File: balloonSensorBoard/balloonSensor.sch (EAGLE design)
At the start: 36 parts, among them IC1 MCP601OT, IC10 MCP601OT, IC6 MCP601OT, IC7 MCP601OT, U1 ARDUINO-MEGAPRO

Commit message: updated .sch, .brd
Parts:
- removed +9V1: 500 ohm, rcl:R-US_R1206
- removed C6, C7: 10uF, resistor:CPOL-EUCT3216
- removed LD1085: (no value), v-reg:LM138-TL
- removed LED3: (no value), SparkFun:LED3MM
- removed U$3: XBEE-1B3, SparkFun:XBEE-1B3
- added C2: 100nF, resistor:CPOL-EUCT3216
- added C3: 10uF, resistor:CPOL-EUCT3216
- added JP1: (no value), SparkFun:M04LONGPADS
- added LD1117: V_REG_317SMD, SparkFun:V_REG_317SMD
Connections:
- removed net N$19: +9V1.2, LED3.C
- net +3V3: now also JP1.1, U1.3.3V; no longer U$3.VDD
- net +9V: now also C2.+, LD1117.IN, U1.VIN; no longer C6.+, LD1085.IN
- net GND: now also C2.-, C3.-, JP1.4, LD1117.ADJ, U1.GND@4; no longer +9V1.1, C6.-, C7.-, LD1085.ADJ, U$3.GND
- net N$13: now also JP1.3; no longer U$3.DIN
- net N$5: now also JP1.2; no longer U$3.DOUT
- net V+: now also C3.+, LD1117.OUT; no longer C7.+, LD1085.OUT, LED3.A
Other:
- note added: "1.8v"
- note added: "XBee"
- note added: "temp/humidity"
- moved on the sheet: C1, JP4, R1, R4

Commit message: added sensors and miscellaneous parts and routed board
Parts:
- removed IC1, IC10, IC6, IC7: MCP601OT, linear:MCP601OT
- removed JP5: (no value), SparkFun:M04LONGPADS
- removed JP6: (no value), jumper:JP1Q
- removed TP1, TP2: TPPAD1-13Y, testpad:TPPAD1-13Y
- added BAROMETER: (no value), SparkFun:M07LONGPADS
- added COMPASS: COMPASS, balloonshield:COMPASS
- added R6: 1k, rcl:R-US_R1206
- renumbered JP1 to XBEE, JP2 to WINDSPEED, JP4 to DUST, U$1 to VOC, U$13 to CO, U$14 to TEMP/HUMIDITY, U$9 to O3
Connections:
- removed net N$12: JP5.3, U1.20(SDA)
- removed net N$20: JP5.4, U1.21(SCL)
- removed net N$48: IC10.-IN, IC10.OUT, U1.A1(TX0)
- removed net N$52: IC6.-IN, IC6.OUT, U1.A0(RX0)
- removed net N$9: IC7.-IN, IC7.OUT, U1.A2
- new net 5V: R1.2, TEMP/HUMIDITY.VDD, U1.5V@0, U1.5V@1, U1.5V@2
- new net SCL: BAROMETER.3, COMPASS.SCL, U1.21(SCL)
- new net SDA: BAROMETER.4, COMPASS.SDA, U1.20(SDA)
- net +3V3: no longer JP5.2
- net +9V: now also BAROMETER.1, COMPASS.VIN
- net GND: now also BAROMETER.7, COMPASS.GND; no longer IC1.V-, IC10.V-, IC6.V-, IC7.V-, JP5.1, TP2.TP
- net N$2: now also U1.A3; no longer IC1.+IN
- net N$4: now also R6.1, U1.AREF; no longer IC1.-IN, IC1.OUT, U1.A3
- net N$47: now also U1.A1(TX0); no longer IC10.+IN
- net N$50: now also U1.A0(RX0); no longer IC6.+IN
- net N$55: now also U1.A2; no longer IC7.+IN
- net V+: now also R6.2; no longer IC1.V+, IC10.V+, IC6.V+, IC7.V+, JP6.1, JP6.2, R1.2, TEMP/HUMIDITY.VDD, TP1.TP
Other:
- note added: "VOC"
- note added: "barometer (altitude)"
- note added: "compass (wind direction)"
- note added: "wind speed"
- note removed: "V+/5V TEST PADS"
- note removed: "compass"
- note removed: "wind"

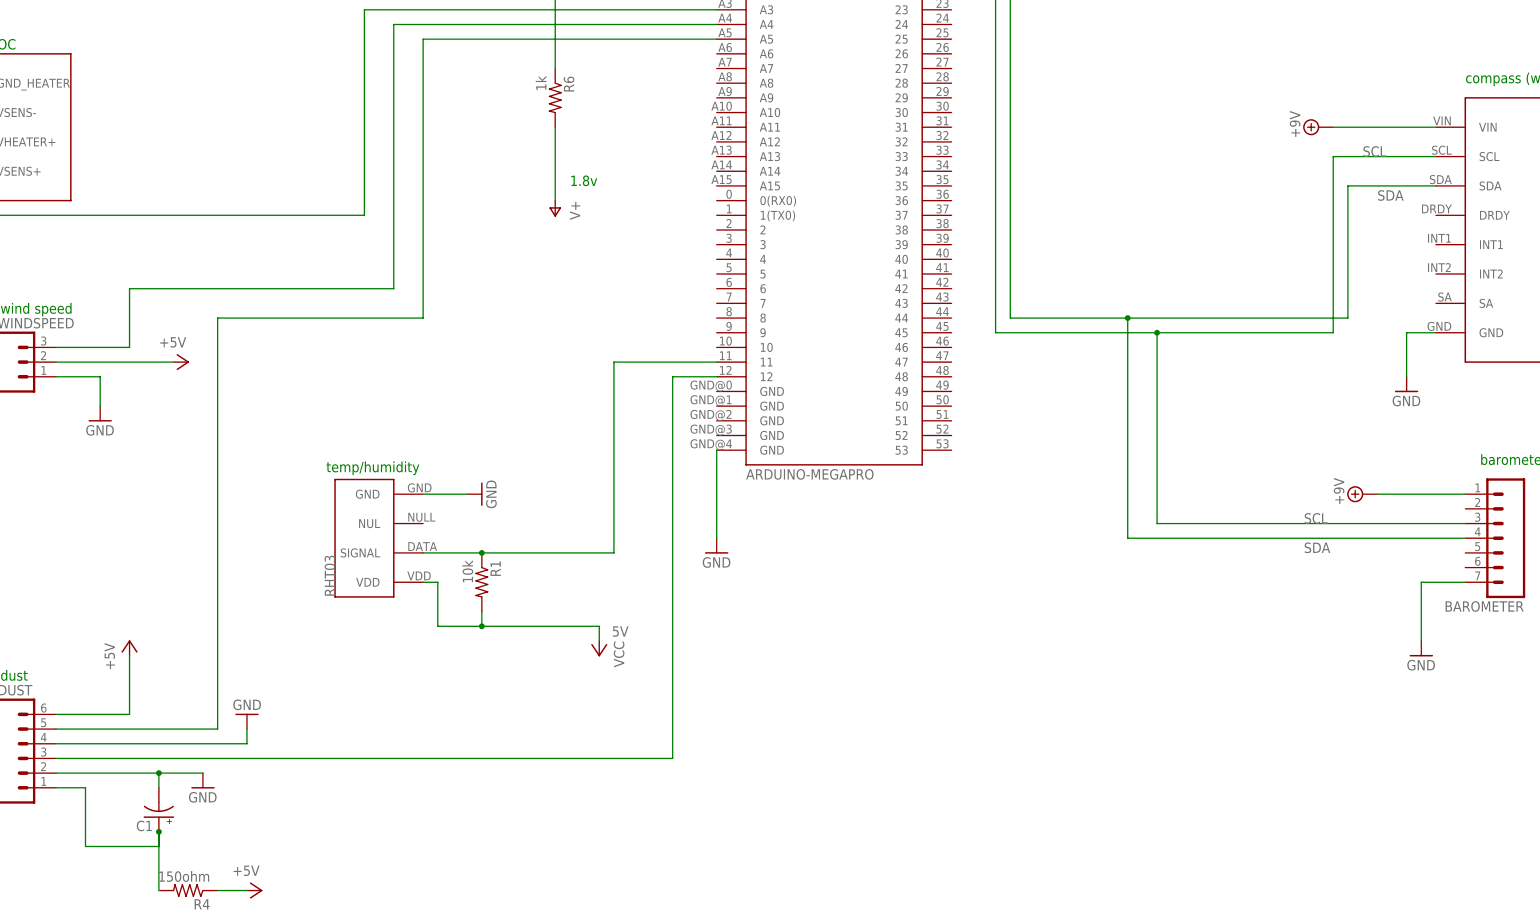
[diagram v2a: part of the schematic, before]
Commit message: added cap size, mod a couple vins
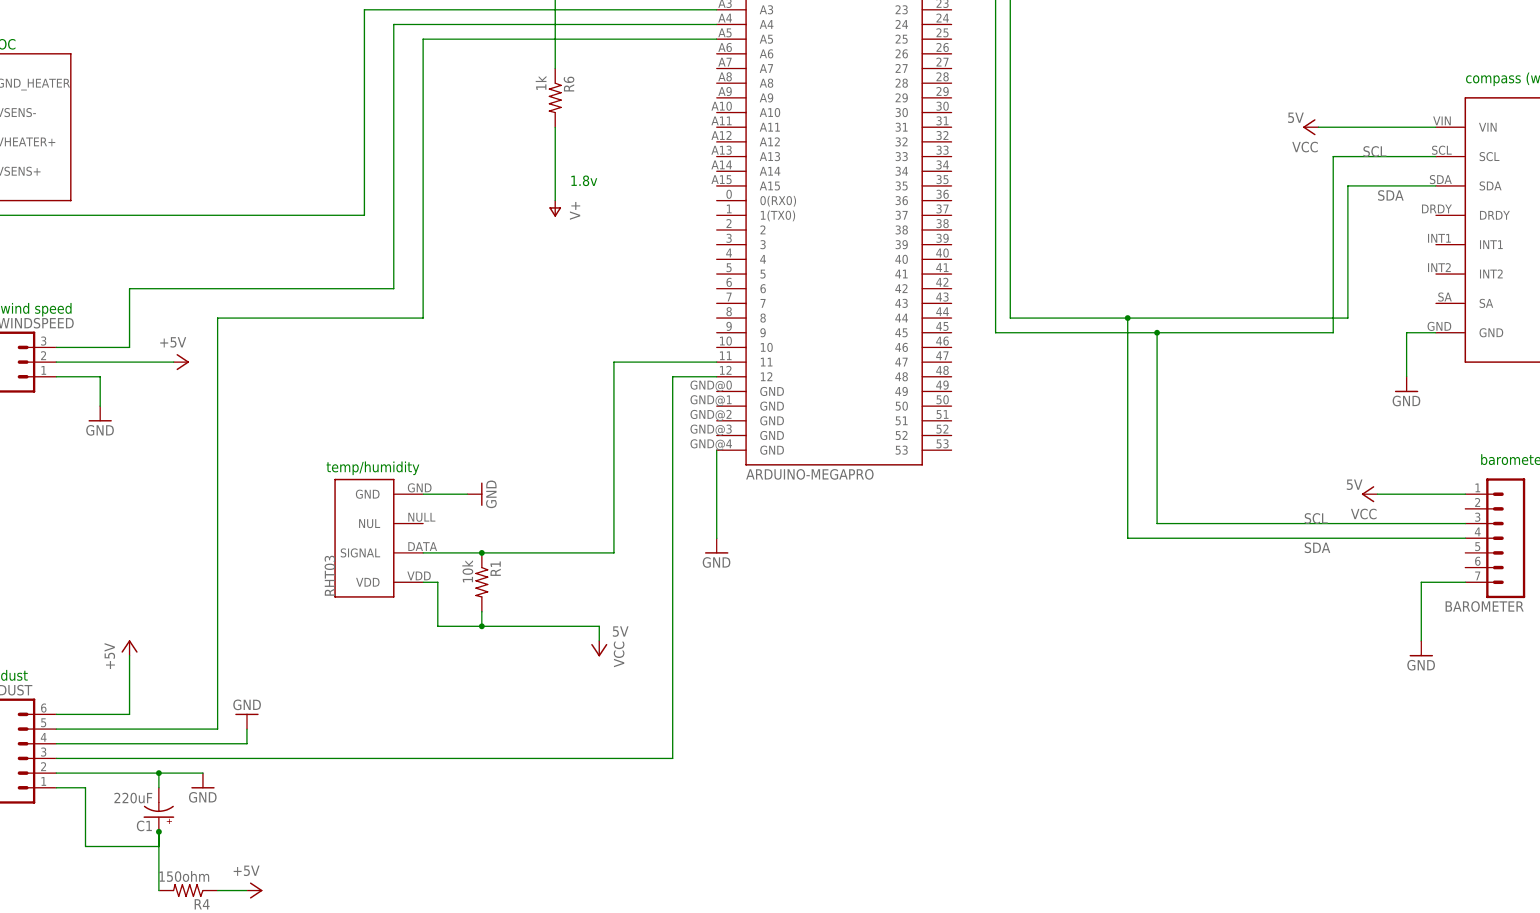
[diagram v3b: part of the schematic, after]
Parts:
- C1: value (none) -> 220uF
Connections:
- new net VCC: BAROMETER.1, COMPASS.VIN
- net +9V: no longer BAROMETER.1, COMPASS.VIN
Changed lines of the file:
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@@
 <part name="GND10" library="supply1" deviceset="GND" device=""/>
 <part name="R4" library="rcl" deviceset="R-US_" device="R1206" value="150ohm"/>
-<part name="C1" library="SparkFun" deviceset="CAP_POL" device="7343"/>
+<part name="C1" library="SparkFun" deviceset="CAP_POL" device="7343" value="220uF"/>
 <part name="GND11" library="supply1" deviceset="GND" device=""/>
 <part name="+3V2" library="supply1" deviceset="+3V3" device=""/>
@@
 <part name="COMPASS" library="balloonshield" deviceset="COMPASS" device=""/>
 <part name="5V" library="supply1" deviceset="VCC" device=""/>
-<part name="SUPPLY4" library="supply2" deviceset="+9V" device=""/>
-<part name="SUPPLY5" library="supply2" deviceset="+9V" device=""/>
 <part name="GND1" library="supply1" deviceset="GND" device=""/>
 <part name="5V1" library="supply1" deviceset="VCC" device=""/>
 <part name="P+1" library="supply1" deviceset="V+" device=""/>
 <part name="R6" library="rcl" deviceset="R-US_" device="R1206" value="1k"/>
+<part name="5V2" library="supply1" deviceset="VCC" device=""/>
+<part name="5V3" library="supply1" deviceset="VCC" device=""/>
 </parts>
 <sheets>
@@
 <instance part="COMPASS" gate="G$1" x="294.64" y="106.68"/>
 <instance part="5V" gate="VCC" x="137.16" y="160.02"/>
-<instance part="SUPPLY4" gate="G$1" x="271.78" y="53.34" rot="R90"/>
-<instance part="SUPPLY5" gate="G$1" x="264.16" y="116.84" rot="R90"/>
 <instance part="GND1" gate="1" x="281.94" y="25.4"/>
 <instance part="5V1" gate="VCC" x="139.7" y="25.4" rot="R180"/>
 <instance part="P+1" gate="1" x="132.08" y="101.6" rot="R180"/>
 <instance part="R6" gate="G$1" x="132.08" y="121.92" rot="R270"/>
+<instance part="5V2" gate="VCC" x="271.78" y="53.34" rot="R90"/>
+<instance part="5V3" gate="VCC" x="261.62" y="116.84" rot="R90"/>
 </instances>
 <busses>
@@
 <wire x1="302.26" y1="256.54" x2="294.64" y2="256.54" width="0.1524" layer="91"/>
 <junction x="294.64" y="256.54"/>
-</segment>
-<segment>
-<pinref part="SUPPLY4" gate="G$1" pin="+9V"/>
-<wire x1="274.32" y1="53.34" x2="289.56" y2="53.34" width="0.1524" layer="91"/>
-<pinref part="BAROMETER" gate="G$1" pin="1"/>
-</segment>
-<segment>
-<pinref part="SUPPLY5" gate="G$1" pin="+9V"/>
-<wire x1="266.7" y1="116.84" x2="284.48" y2="116.84" width="0.1524" layer="91"/>
-<pinref part="COMPASS" gate="G$1" pin="VIN"/>
 </segment>
 </net>
@@
 <wire x1="111.76" y1="30.48" x2="119.38" y2="30.48" width="0.1524" layer="91"/>
 <junction x="119.38" y="30.48"/>
+<label x="271.78" y="55.88" size="1.778" layer="95" rot="R180"/>
+<label x="261.62" y="119.38" size="1.778" layer="95" rot="R180"/>
 </segment>
 </net>
@@
 </segment>
 </net>
+<net name="VCC" class="0">
+<segment>
+<wire x1="274.32" y1="53.34" x2="289.56" y2="53.34" width="0.1524" layer="91"/>
+<pinref part="BAROMETER" gate="G$1" pin="1"/>
+<pinref part="5V2" gate="VCC" pin="VCC"/>
+</segment>
+<segment>
+<wire x1="264.16" y1="116.84" x2="284.48" y2="116.84" width="0.1524" layer="91"/>
+<pinref part="COMPASS" gate="G$1" pin="VIN"/>
+<pinref part="5V3" gate="VCC" pin="VCC"/>
+</segment>
+</net>

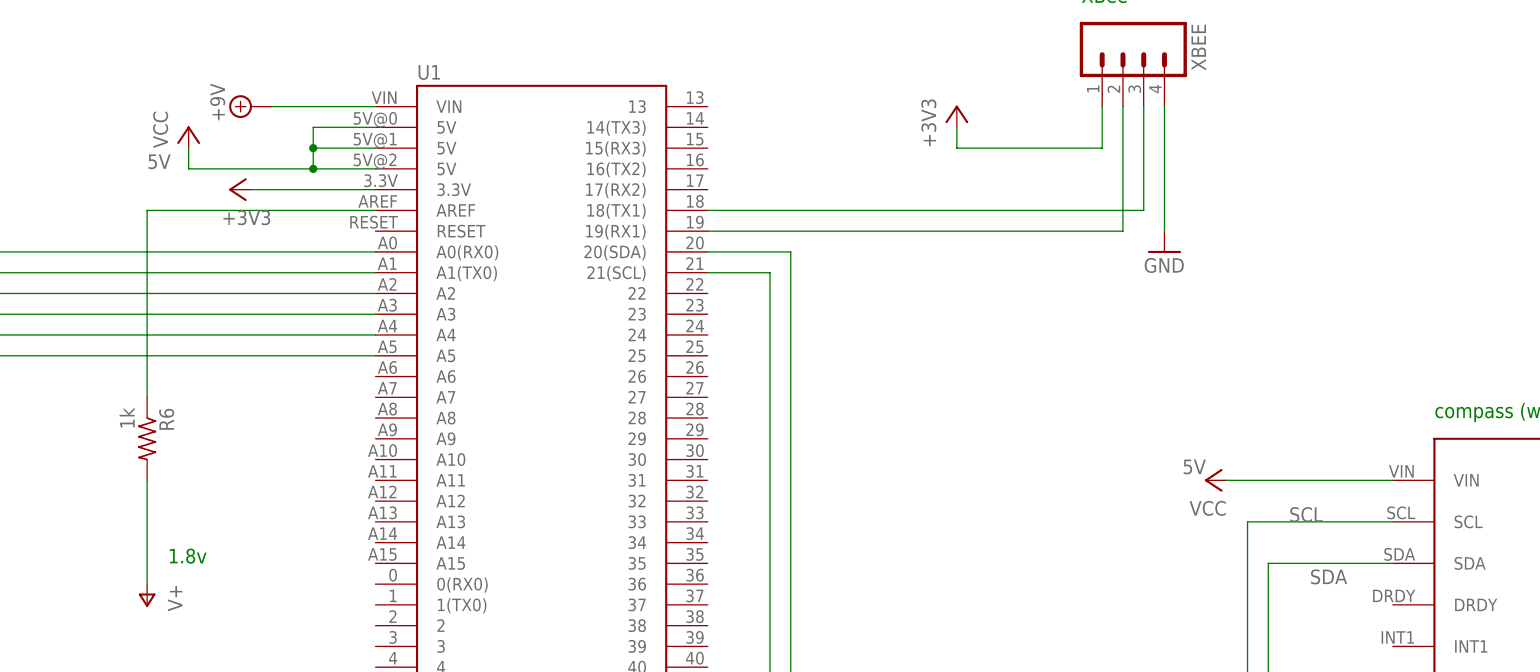
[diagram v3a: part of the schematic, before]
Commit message: added top copper text
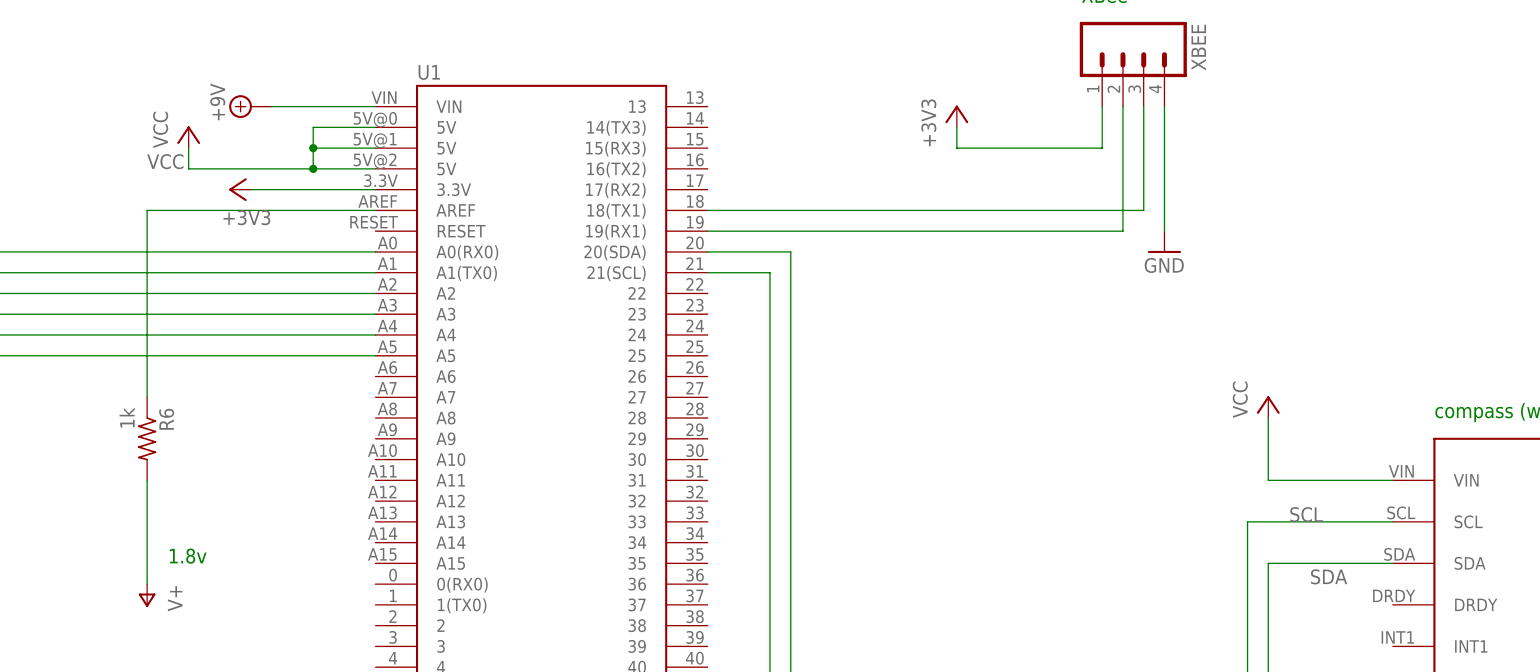
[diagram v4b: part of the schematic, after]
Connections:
- net 5V: no longer U1.5V@0, U1.5V@1, U1.5V@2
- net VCC: now also U1.5V@0, U1.5V@1, U1.5V@2
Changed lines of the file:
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@@
 <part name="R6" library="rcl" deviceset="R-US_" device="R1206" value="1k"/>
 <part name="5V2" library="supply1" deviceset="VCC" device=""/>
-<part name="5V3" library="supply1" deviceset="VCC" device=""/>
+<part name="5V4" library="supply1" deviceset="VCC" device=""/>
 </parts>
 <sheets>
@@
 <instance part="R6" gate="G$1" x="132.08" y="121.92" rot="R270"/>
 <instance part="5V2" gate="VCC" x="271.78" y="53.34" rot="R90"/>
-<instance part="5V3" gate="VCC" x="261.62" y="116.84" rot="R90"/>
+<instance part="5V4" gate="VCC" x="269.24" y="127"/>
 </instances>
 <busses>
@@
 <net name="5V" class="0">
 <segment>
+<wire x1="139.7" y1="30.48" x2="139.7" y2="27.94" width="0.1524" layer="91"/>
+<pinref part="5V1" gate="VCC" pin="VCC"/>
+<label x="144.78" y="30.48" size="1.778" layer="95" rot="R180"/>
+<pinref part="R1" gate="G$1" pin="2"/>
+<wire x1="139.7" y1="30.48" x2="119.38" y2="30.48" width="0.1524" layer="91"/>
+<wire x1="119.38" y1="30.48" x2="119.38" y2="33.02" width="0.1524" layer="91"/>
+<pinref part="TEMP/HUMIDITY" gate="G$1" pin="VDD"/>
+<wire x1="109.22" y1="38.1" x2="111.76" y2="38.1" width="0.1524" layer="91"/>
+<wire x1="111.76" y1="38.1" x2="111.76" y2="30.48" width="0.1524" layer="91"/>
+<wire x1="111.76" y1="30.48" x2="119.38" y2="30.48" width="0.1524" layer="91"/>
+<junction x="119.38" y="30.48"/>
+<label x="271.78" y="55.88" size="1.778" layer="95" rot="R180"/>
+</segment>
+</net>
+<net name="N$4" class="0">
+<segment>
+<pinref part="U1" gate="G$1" pin="AREF"/>
+<wire x1="160.02" y1="149.86" x2="132.08" y2="149.86" width="0.1524" layer="91"/>
+<wire x1="132.08" y1="149.86" x2="132.08" y2="127" width="0.1524" layer="91"/>
+<pinref part="R6" gate="G$1" pin="1"/>
+</segment>
+</net>
+<net name="VCC" class="0">
+<segment>
+<wire x1="274.32" y1="53.34" x2="289.56" y2="53.34" width="0.1524" layer="91"/>
+<pinref part="BAROMETER" gate="G$1" pin="1"/>
+<pinref part="5V2" gate="VCC" pin="VCC"/>
+</segment>
+<segment>
+<pinref part="COMPASS" gate="G$1" pin="VIN"/>
+<wire x1="269.24" y1="116.84" x2="284.48" y2="116.84" width="0.1524" layer="91"/>
+<pinref part="5V4" gate="VCC" pin="VCC"/>
+<wire x1="269.24" y1="124.46" x2="269.24" y2="116.84" width="0.1524" layer="91"/>
+</segment>
+<segment>
 <pinref part="U1" gate="G$1" pin="5V@2"/>
 <wire x1="160.02" y1="154.94" x2="152.4" y2="154.94" width="0.1524" layer="91"/>
@@
 <junction x="152.4" y="157.48"/>
 </segment>
-<segment>
-<wire x1="139.7" y1="30.48" x2="139.7" y2="27.94" width="0.1524" layer="91"/>
-<pinref part="5V1" gate="VCC" pin="VCC"/>
-<label x="144.78" y="30.48" size="1.778" layer="95" rot="R180"/>
-<pinref part="R1" gate="G$1" pin="2"/>
-<wire x1="139.7" y1="30.48" x2="119.38" y2="30.48" width="0.1524" layer="91"/>
-<wire x1="119.38" y1="30.48" x2="119.38" y2="33.02" width="0.1524" layer="91"/>
-<pinref part="TEMP/HUMIDITY" gate="G$1" pin="VDD"/>
-<wire x1="109.22" y1="38.1" x2="111.76" y2="38.1" width="0.1524" layer="91"/>
-<wire x1="111.76" y1="38.1" x2="111.76" y2="30.48" width="0.1524" layer="91"/>
-<wire x1="111.76" y1="30.48" x2="119.38" y2="30.48" width="0.1524" layer="91"/>
-<junction x="119.38" y="30.48"/>
-<label x="271.78" y="55.88" size="1.778" layer="95" rot="R180"/>
-<label x="261.62" y="119.38" size="1.778" layer="95" rot="R180"/>
-</segment>
-</net>
-<net name="N$4" class="0">
-<segment>
-<pinref part="U1" gate="G$1" pin="AREF"/>
-<wire x1="160.02" y1="149.86" x2="132.08" y2="149.86" width="0.1524" layer="91"/>
-<wire x1="132.08" y1="149.86" x2="132.08" y2="127" width="0.1524" layer="91"/>
-<pinref part="R6" gate="G$1" pin="1"/>
-</segment>
-</net>
-<net name="VCC" class="0">
-<segment>
-<wire x1="274.32" y1="53.34" x2="289.56" y2="53.34" width="0.1524" layer="91"/>
-<pinref part="BAROMETER" gate="G$1" pin="1"/>
-<pinref part="5V2" gate="VCC" pin="VCC"/>
-</segment>
-<segment>
-<wire x1="264.16" y1="116.84" x2="284.48" y2="116.84" width="0.1524" layer="91"/>
-<pinref part="COMPASS" gate="G$1" pin="VIN"/>
-<pinref part="5V3" gate="VCC" pin="VCC"/>
-</segment>
-</net>
+</net>

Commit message: updated resistors
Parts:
- R31: value 60 ohm -> 80 ohm
- R7: value 34 ohm -> 120 ohm
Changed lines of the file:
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@@
 <part name="R5" library="rcl" deviceset="R-US_" device="R1206" value="220k"/>
 <part name="GND27" library="supply1" deviceset="GND" device=""/>
-<part name="R7" library="rcl" deviceset="R-US_" device="R1206" value="34 ohm"/>
+<part name="R7" library="rcl" deviceset="R-US_" device="R1206" value="120 ohm"/>
 <part name="P+6" library="supply1" deviceset="V+" device=""/>
 <part name="O3" library="ricardo" deviceset="E2V" device="" value="E2V Ozone"/>
@@
 <part name="R30" library="rcl" deviceset="R-US_" device="R1206" value="220k"/>
 <part name="GND33" library="supply1" deviceset="GND" device=""/>
-<part name="R31" library="rcl" deviceset="R-US_" device="R1206" value="60 ohm"/>
+<part name="R31" library="rcl" deviceset="R-US_" device="R1206" value="80 ohm"/>
 <part name="P+12" library="supply1" deviceset="V+" device=""/>
 <part name="SUPPLY16" library="supply2" deviceset="+9V" device=""/>
